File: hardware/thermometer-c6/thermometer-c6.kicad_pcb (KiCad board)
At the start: 2 copper layers, 48 x 35 mm, 101 parts, among them J1 JST-PH-2 BAT, J2 MEAS_HDR, J3 USB-C, J4 EPD FPC24 0.5mm, J5 DEBUG, Q1 AO3401A, Q2 AO3401A, Q3 Si1308EDL, Q4 AO3401A, Q5 2N7002, Q6 AO3401A, SW1 RESET, SW2 BOOT, U1 ESP32-C6-MINI-1-N4, U2 RT9080-33GJ5, U3 USBLC6-2SC6, U4 MCP73831-2, U5 BMP581, U6 BMP585, Y1 32.768kHz FC-135

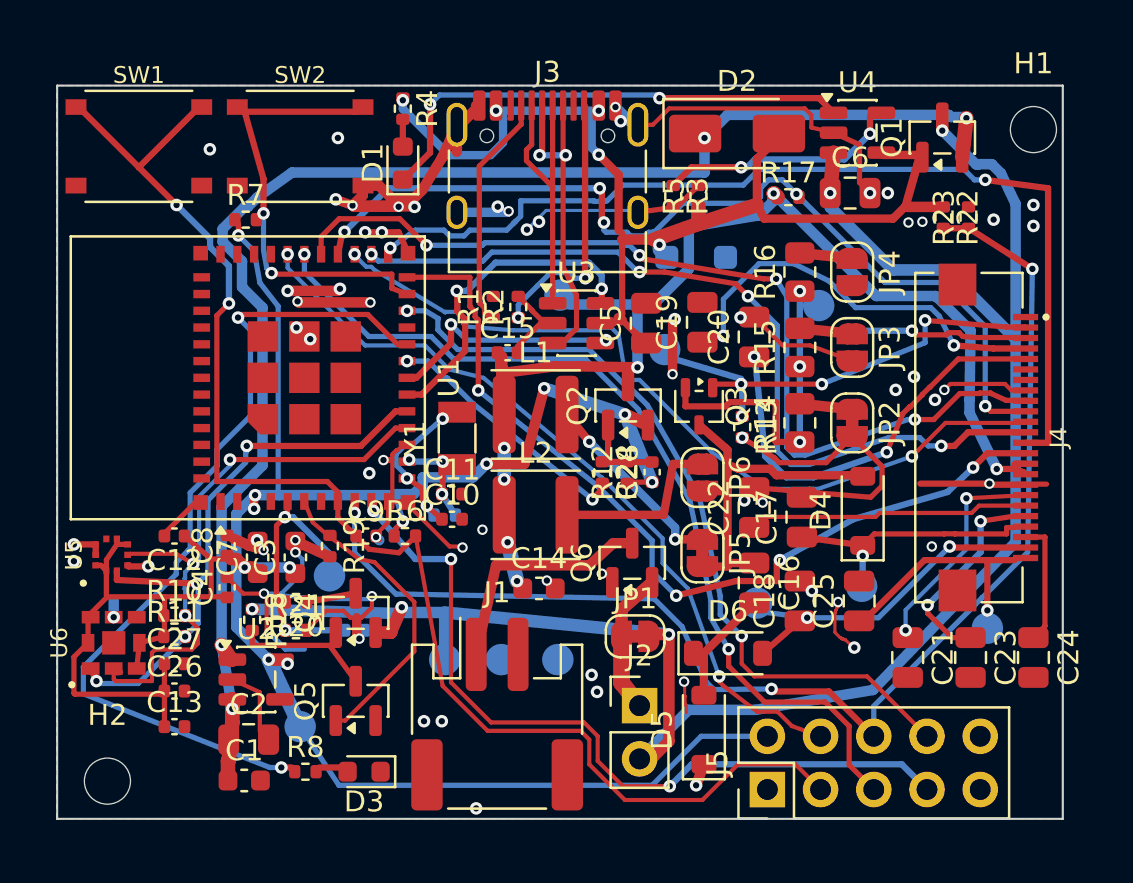
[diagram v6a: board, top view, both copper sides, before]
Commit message: Harvest widen + antenna cleanup; trim 3 stubs; straighten to fixpoint
User widened all sub-0.25mm traces to >=0.25 (min now 0.25) and cleaned up LED_STATUS/SDA/SCL near the antenna B side; the 27-pad B.Cu GND neck went 0.15->0.25 (still single-path). Harvested 34 signal nets + GND (STITCH 68, 40 grown 0.6/0.3 preserved; TRACKS 44). Trimmed 3 dangling stubs (EN/VDIV_EN/LED_STATUS -> track_dangling 0). Scripted straighten to fixpoint: -50 verts/-7.54mm (no widen -- widths are user-managed). DRC REAL=0/unconnected=0/starved=0, gnd_islands 1 island, make check green, byte-stable; out/hand-vs-generated differs only by the trim+straighten.

Co-Authored-By: Claude Opus 4.8 (1M context) <noreply@anthropic.com>
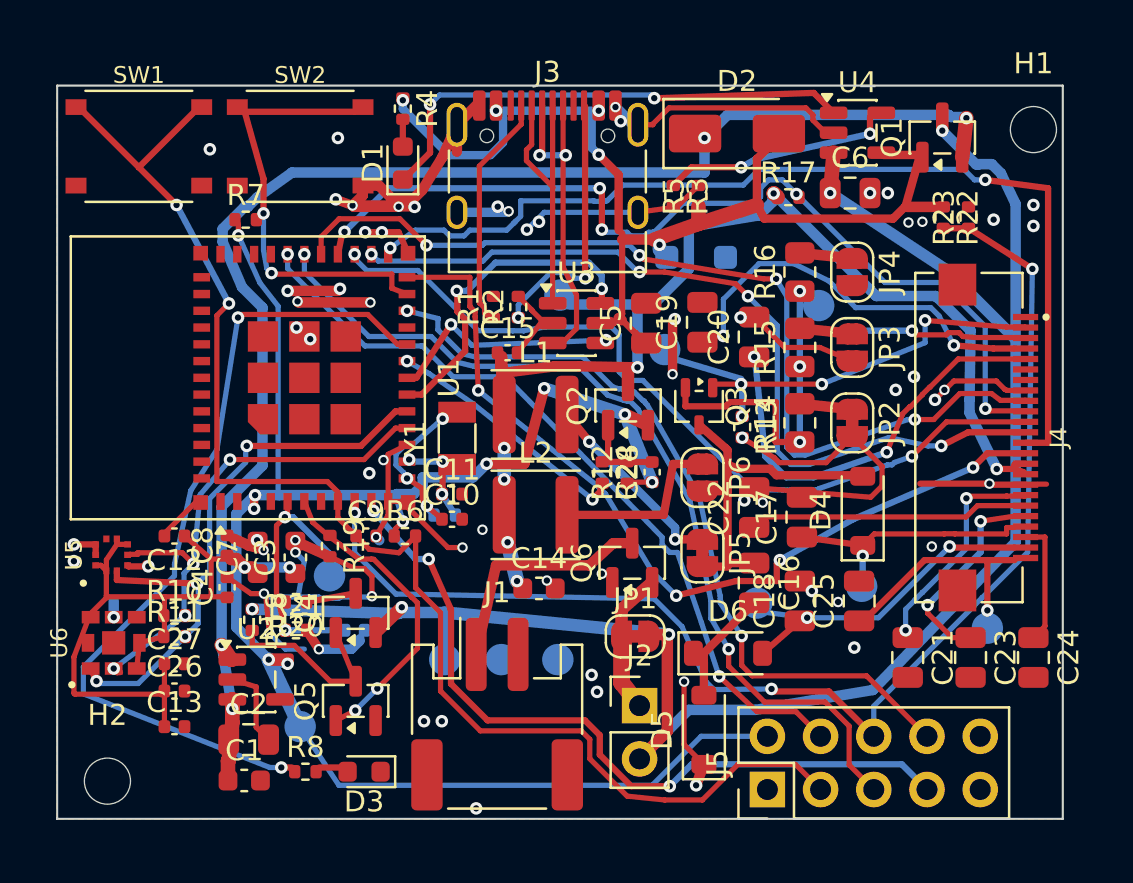
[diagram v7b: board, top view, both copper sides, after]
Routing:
- net GND: track 142.7 -> 138.2 mm
- net SDA: track 28.6 -> 25.1 mm, vias 3 -> 4
- net Net-(Q4-G): track 6.52 -> 8.87 mm
- net VBAT: track 89.9 -> 88.4 mm
- net LED_STATUS: track 40.8 -> 39.6 mm
- net DBG_IO5: track 37.5 -> 36.4 mm
- net EPD_DC: track 38.4 -> 38.9 mm
- net EPD_MOSI: track 41.8 -> 41.3 mm
- net VDIV_EN: track 14.8 -> 15.0 mm, vias 0 -> 2

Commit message: Add east-cap redundant GND via to resolve 15-pad SPOF
via@(44.70,6.40) was the sole GND tie for the 15-pad east cap/connector cluster (C17-C25, C5/C6, D7, J4.8/17, JP2.2). A 2nd 0.5/0.3 stitch at board-rel (44.49,5.58) gives it two independent ties. gnd_islands: 15-pad single-via SPOF resolved (single-via ties now 4x 1-pad inherent keep-out ties). DRC REAL=0, make check green, byte-stable.

Co-Authored-By: Claude Opus 4.8 (1M context) <noreply@anthropic.com>
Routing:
- net GND: vias 68 -> 69
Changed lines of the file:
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@@
+	)
+	(via
+		(at 144.49 105.58)
+		(size 0.5)
+		(drill 0.3)
+		(layers "F.Cu" "B.Cu")
+		(net "GND")
 	)
 	(via
